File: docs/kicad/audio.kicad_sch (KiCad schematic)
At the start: 0 parts

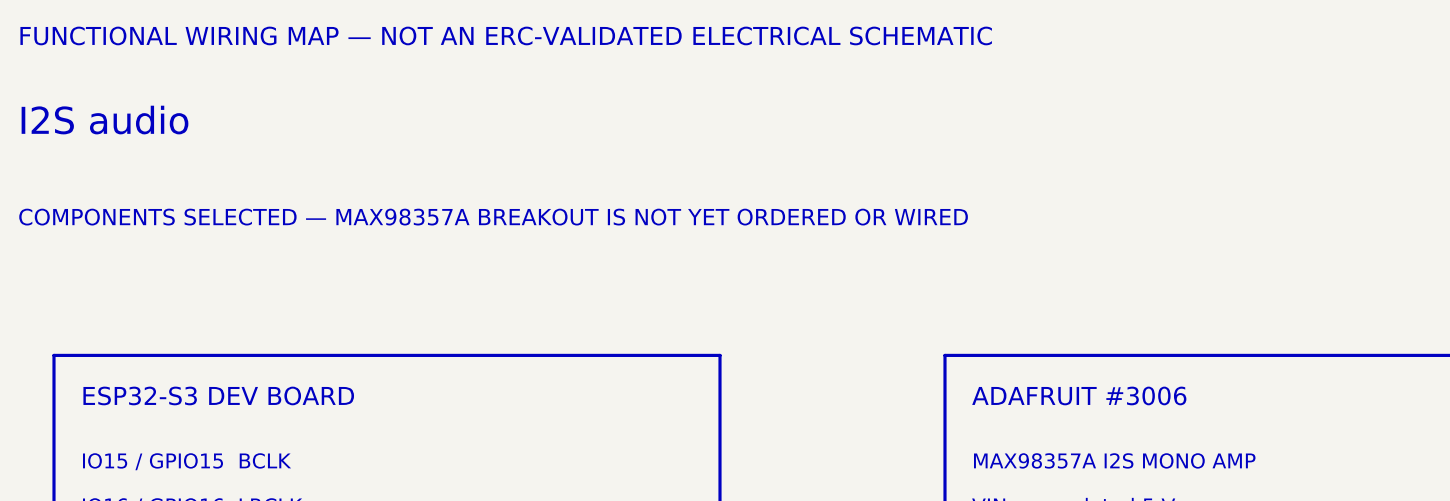
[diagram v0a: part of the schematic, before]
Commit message: docs: remove hardware procurement status
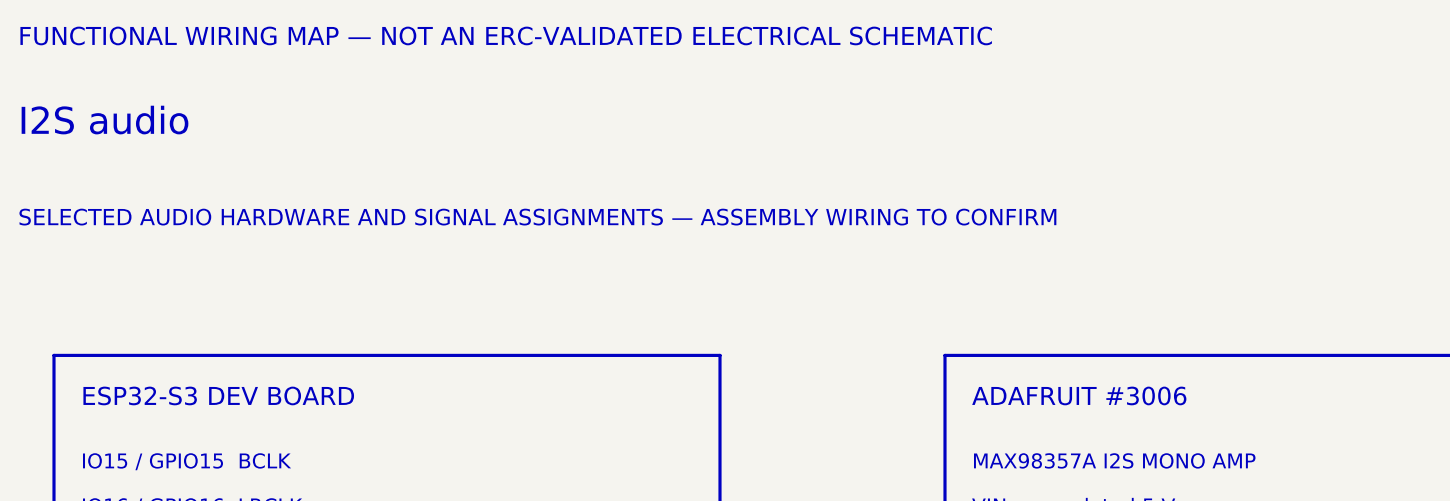
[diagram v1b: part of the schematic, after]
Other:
- note added: "SELECTED AUDIO HARDWARE AND SIGNAL ASSIGNMENTS — ASSEMBLY WIRING TO CONFIRM"
- note removed: "COMPONENTS SELECTED — MAX98357A BREAKOUT IS NOT YET ORDERED OR WIRED"
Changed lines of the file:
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@@
   (text "FUNCTIONAL WIRING MAP — NOT AN ERC-VALIDATED ELECTRICAL SCHEMATIC" (at 16 18 0) (effects (font (size 2.0 2.0)) (justify left bottom)))
   (text "I2S audio" (at 16 28 0) (effects (font (size 3.0 3.0)) (justify left bottom)))
-  (text "COMPONENTS SELECTED — MAX98357A BREAKOUT IS NOT YET ORDERED OR WIRED" (at 16 38 0) (effects (font (size 1.8 1.8)) (justify left bottom)))
+  (text "SELECTED AUDIO HARDWARE AND SIGNAL ASSIGNMENTS — ASSEMBLY WIRING TO CONFIRM" (at 16 38 0) (effects (font (size 1.8 1.8)) (justify left bottom)))
   (polyline (pts (xy 20 52) (xy 94 52) (xy 94 95) (xy 20 95) (xy 20 52)) (stroke (width 0.35) (type default)) (fill (type none)))
   (text "ESP32-S3 DEV BOARD" (at 23 58 0) (effects (font (size 2.0 2.0)) (justify left bottom)))
